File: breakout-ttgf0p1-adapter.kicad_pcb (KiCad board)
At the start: 4 copper layers, 50 x 50 mm, 115 parts, among them J1 Conn_01x12, J2 Conn_02x08_Odd_Even, J3 DF12NB-60DS-0.5V_51, J4 Conn_02x08_Odd_Even, J5 DF12NB-50DS-0.5V_51, J6 Conn_02x08_Odd_Even, J8 Conn_02x08_Odd_Even, U1 AP2112K-3.3, U2 AP2112K-3.3, U4 24LC02

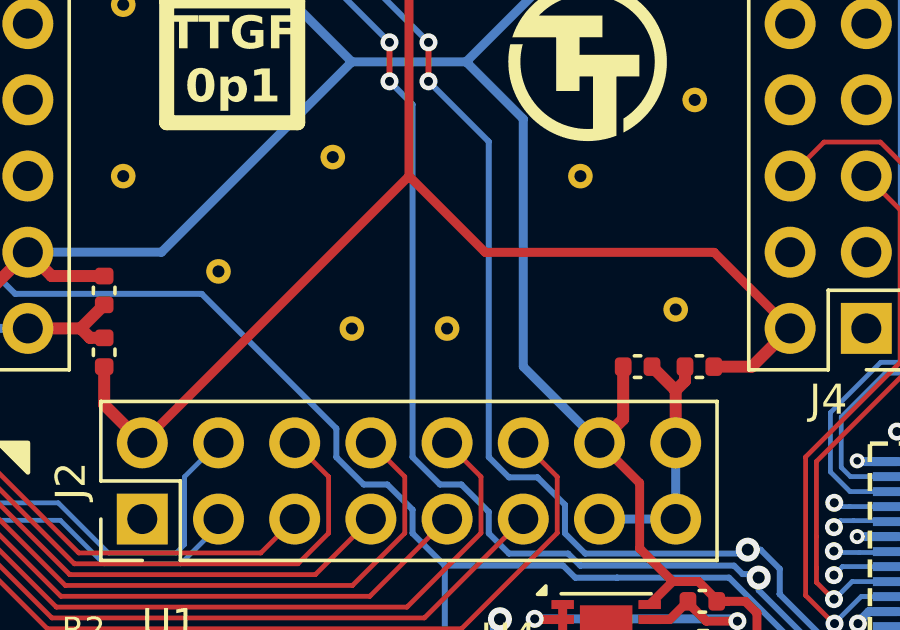
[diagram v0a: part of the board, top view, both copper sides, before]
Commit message: add tillitis logo
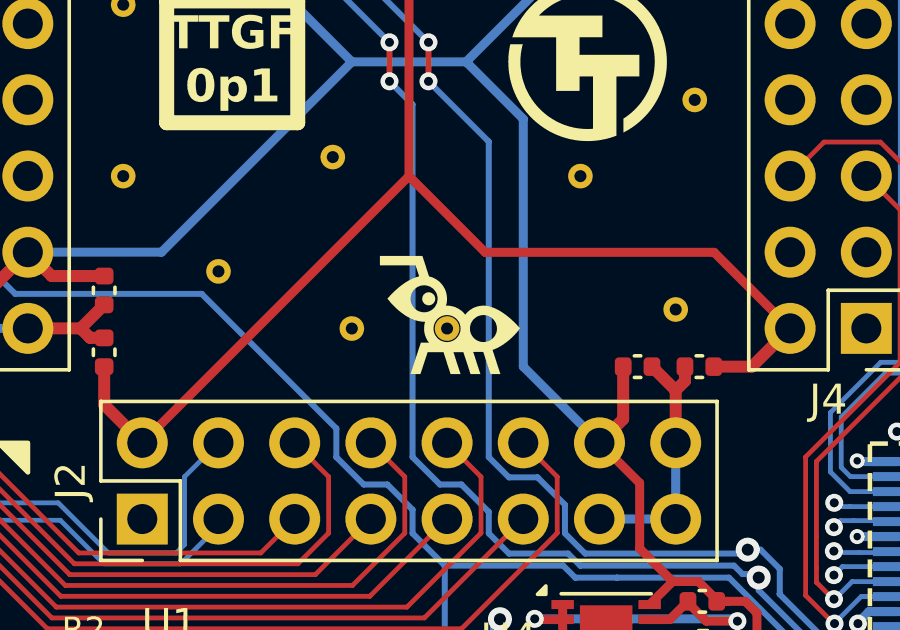
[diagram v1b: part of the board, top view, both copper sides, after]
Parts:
- added TILL1: Tillitis_logo, Logos:tillitis_logo, F.Cu at (140.3, 75.1)

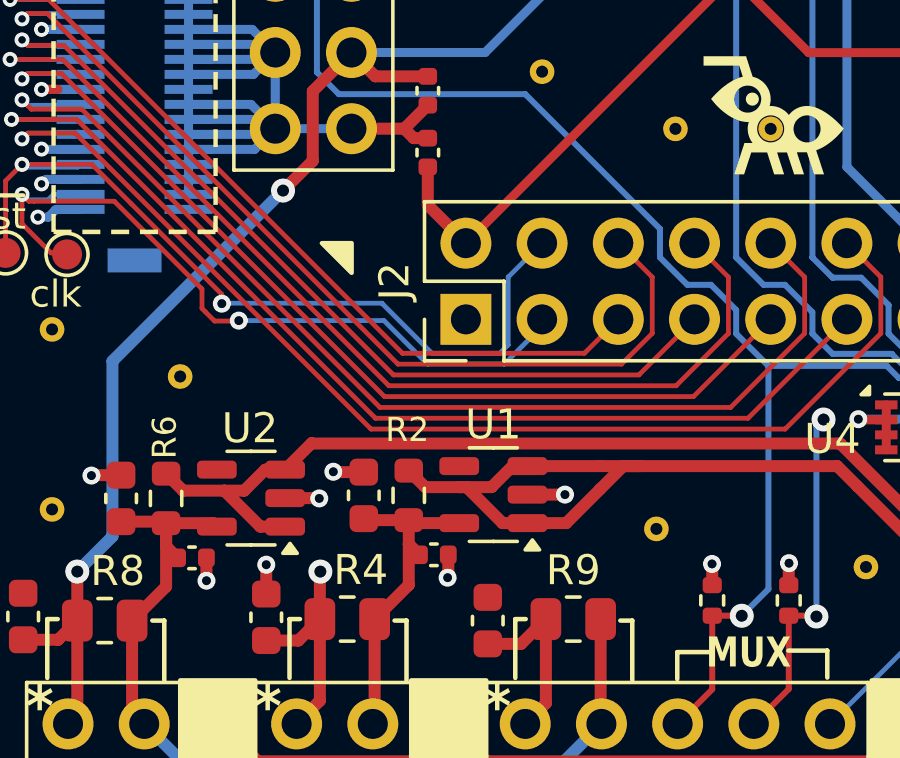
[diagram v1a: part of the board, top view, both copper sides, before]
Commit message: don't remove duplicate track
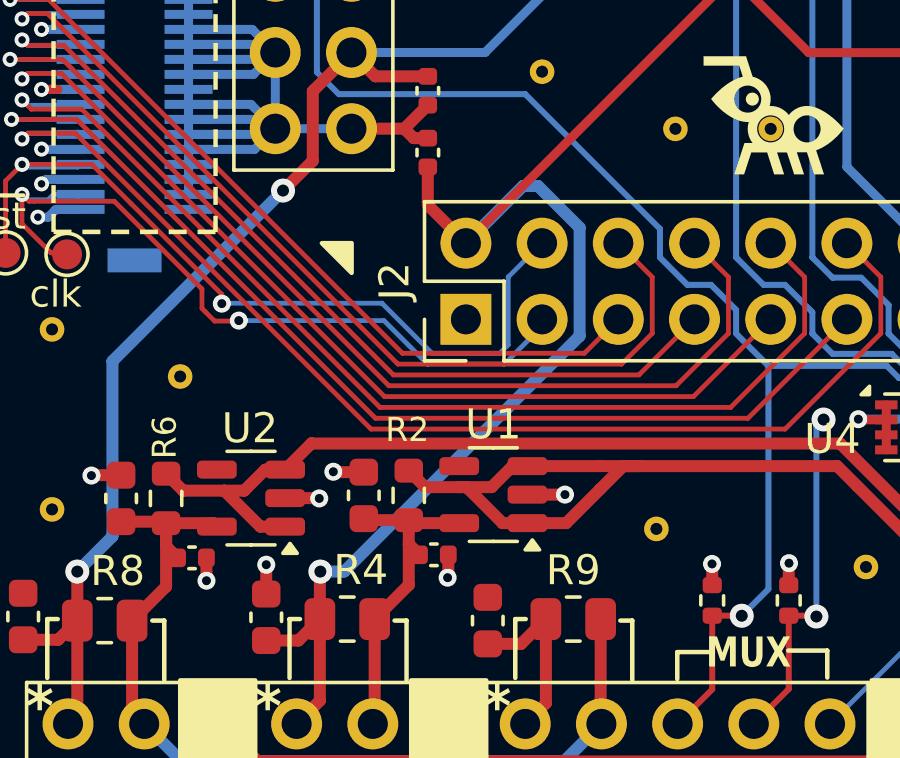
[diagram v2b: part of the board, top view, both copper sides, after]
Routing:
- net VDD_{CORE}: track 95.1 -> 115.8 mm
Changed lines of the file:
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@@
+	(segment
+		(start 125.1936 90.3224)
+		(end 125.984781 90.3224)
+		(width 0.4)
+		(layer "B.Cu")
+		(net 6)
+	)
+	(segment
+		(start 133.836 82.471181)
+		(end 133.836 78.856818)
+		(width 0.4)
+		(layer "B.Cu")
+		(net 6)
+	)
+	(segment
+		(start 132.449182 77.47)
+		(end 131.95 77.47)
+		(width 0.4)
+		(layer "B.Cu")
+		(net 6)
+	)
+	(segment
+		(start 131.95 77.47)
+		(end 130.045 79.375)
+		(width 0.4)
+		(layer "B.Cu")
+		(net 6)
+	)
+	(segment
+		(start 125.984781 90.3224)
+		(end 133.836 82.471181)
+		(width 0.4)
+		(layer "B.Cu")
+		(net 6)
+	)
+	(segment
+		(start 133.836 78.856818)
+		(end 132.449182 77.47)
+		(width 0.4)
+		(layer "B.Cu")
+		(net 6)
+	)
 	(segment
 		(start 125.1936 90.3224)
